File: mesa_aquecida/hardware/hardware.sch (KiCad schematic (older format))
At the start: 29 parts, among them J1 Conn_01x03_Male, J2 Conn_01x04_Male, J3 Conn_01x04_Male, J4 Conn_01x02_Female, J5 Conn_01x02_Male, J6 Conn_01x02_Male, J7 Conn_01x02_Male, J8 Conn_01x02_Male, J9 Conn_01x02_Female, Q1 2N7002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

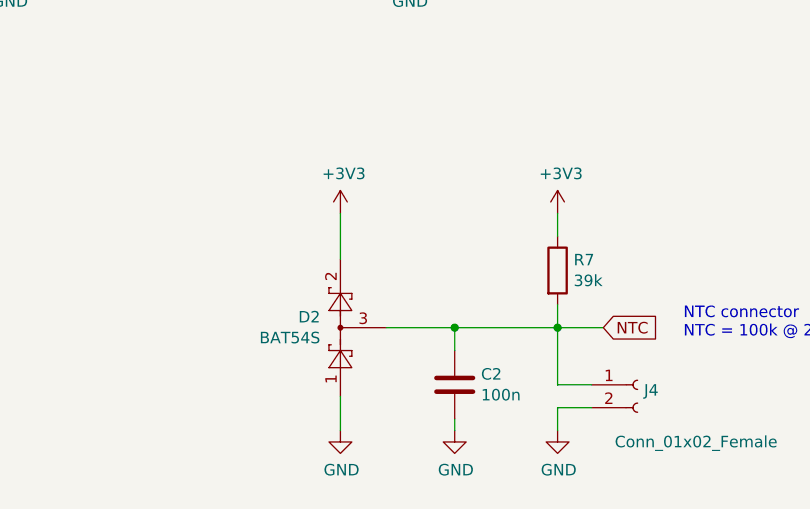
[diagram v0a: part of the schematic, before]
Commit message: updated schematic, removed diodes
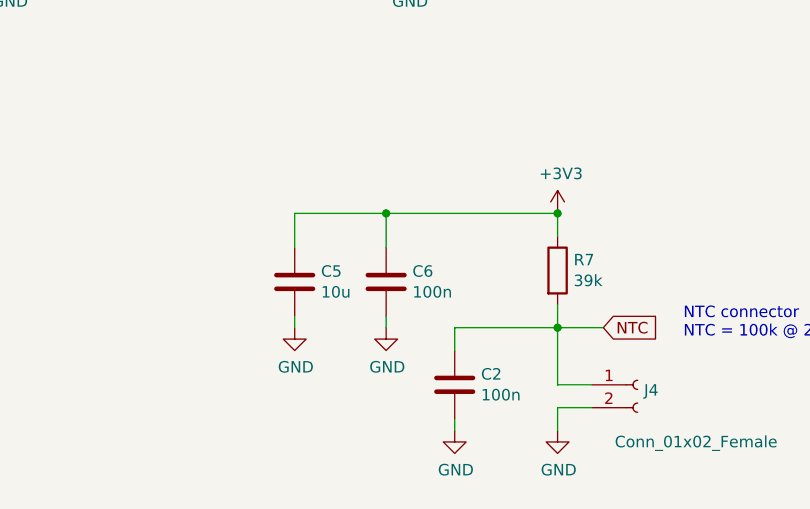
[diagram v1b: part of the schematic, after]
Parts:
- removed D2: BAT54S, Package_TO_SOT_SMD:SOT-23, symbol Diode:BAT54S
- added C5: 10u, symbol Device:C
- added C6: 100n, symbol Device:C
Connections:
- net +3V3: now also C5.1, C6.1
- net GND: now also C5.2, C6.2
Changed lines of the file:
@@
 	1300 5400 1300 5850
-$Comp
-L Diode:BAT54S D2
-U 1 1 6119E775
-P 4100 5950
-F 0 "D2" V 4146 6038 50  0000 L CNN
-F 1 "BAT54S" V 4055 6038 50  0000 L CNN
-F 2 "Package_TO_SOT_SMD:SOT-23" H 4175 6075 50  0001 L CNN
-F 3 "https://www.diodes.com/assets/Datasheets/ds11005.pdf" H 3980 5950 50  0001 C CNN
-	1    4100 5950
-	0    -1   -1   0
-$EndComp
-$Comp
-L power:+3V3 #PWR012
-U 1 1 611A238D
-P 4100 5450
-F 0 "#PWR012" H 4100 5300 50  0001 C CNN
-F 1 "+3V3" H 4115 5623 50  0000 C CNN
-F 2 "" H 4100 5450 50  0001 C CNN
-F 3 "" H 4100 5450 50  0001 C CNN
-	1    4100 5450
-	1    0    0    -1
-$EndComp
-$Comp
-L power:GND #PWR013
-U 1 1 611A28CE
-P 4100 6400
-F 0 "#PWR013" H 4100 6150 50  0001 C CNN
-F 1 "GND" H 4105 6227 50  0000 C CNN
-F 2 "" H 4100 6400 50  0001 C CNN
-F 3 "" H 4100 6400 50  0001 C CNN
-	1    4100 6400
-	1    0    0    -1
-$EndComp
-Wire Wire Line
-	4100 6250 4100 6400
 $Comp
 L Transistor_FET:IRF540N Q2
@@
 	5050 5550 5050 5450
 Wire Wire Line
-	4100 5650 4100 5450
-Wire Wire Line
 	5050 5850 5050 5950
 Connection ~ 5050 5950
@@
 Wire Wire Line
 	5900 3250 6150 3250
-Wire Wire Line
-	4300 5950 4600 5950
 $Comp
 L Device:C C2
@@
 Wire Wire Line
 	4600 6050 4600 5950
-Connection ~ 4600 5950
 Wire Wire Line
 	4600 5950 5050 5950
@@
 Wire Wire Line
 	2900 3650 2400 3650
+$Comp
+L Device:C C6
+U 1 1 61175D0A
+P 4300 5750
+F 0 "C6" H 4415 5796 50  0000 L CNN
+F 1 "100n" H 4415 5705 50  0000 L CNN
+F 2 "" H 4338 5600 50  0001 C CNN
+F 3 "~" H 4300 5750 50  0001 C CNN
+	1    4300 5750
+	1    0    0    -1
+$EndComp
+$Comp
+L Device:C C5
+U 1 1 61176977
+P 3900 5750
+F 0 "C5" H 4015 5796 50  0000 L CNN
+F 1 "10u" H 4015 5705 50  0000 L CNN
+F 2 "" H 3938 5600 50  0001 C CNN
+F 3 "~" H 3900 5750 50  0001 C CNN
+	1    3900 5750
+	1    0    0    -1
+$EndComp
+$Comp
+L power:GND #PWR013
+U 1 1 61176CDE
+P 4300 5950
+F 0 "#PWR013" H 4300 5700 50  0001 C CNN
+F 1 "GND" H 4305 5777 50  0000 C CNN
+F 2 "" H 4300 5950 50  0001 C CNN
+F 3 "" H 4300 5950 50  0001 C CNN
+	1    4300 5950
+	1    0    0    -1
+$EndComp
+$Comp
+L power:GND #PWR012
+U 1 1 61176FB0
+P 3900 5950
+F 0 "#PWR012" H 3900 5700 50  0001 C CNN
+F 1 "GND" H 3905 5777 50  0000 C CNN
+F 2 "" H 3900 5950 50  0001 C CNN
+F 3 "" H 3900 5950 50  0001 C CNN
+	1    3900 5950
+	1    0    0    -1
+$EndComp
+Wire Wire Line
+	4300 5600 4300 5450
+Wire Wire Line
+	4300 5450 5050 5450
+Connection ~ 5050 5450
+Wire Wire Line
+	4300 5450 3900 5450
+Wire Wire Line
+	3900 5450 3900 5600
+Connection ~ 4300 5450
+Wire Wire Line
+	3900 5900 3900 5950
+Wire Wire Line
+	4300 5900 4300 5950
 $EndSCHEMATC

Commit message: Updated PCB
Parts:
- removed J1: Conn_01x03_Male, symbol Connector:Conn_01x03_Male
- removed J9: Conn_01x02_Female, symbol Connector:Conn_01x02_Female
- added HS1: Heatsink, Heatsink:Heatsink_Fischer_SK104-STCB_35x13mm__2xDrill3.5mm_ScrewM3, symbol Mechanical:Heatsink
- added J1, J10: Conn_01x04_Male, Connector_PinHeader_2.54mm:PinHeader_1x04_P2.54mm_Vertical, symbol Connector:Conn_01x04_Male
- added J9: Screw_Terminal_01x03, TerminalBlock:TerminalBlock_bornier-3_P5.08mm, symbol Connector:Screw_Terminal_01x03
- added SW1, SW2, SW3: SW_MEC_5E, Button_Switch_THT:SW_PUSH_6mm, symbol Switch:SW_Push
- C1, C2, C3, C4, C5, C6: footprint (none) -> Capacitor_SMD:C_0805_2012Metric_Pad1.18x1.45mm_HandSolder
- D1, D3: footprint (none) -> Diode_SMD:D_SMB
- J2, J3: footprint (none) -> Connector_PinHeader_2.54mm:PinHeader_1x04_P2.54mm_Vertical
- J4, J5, J6, J7, J8: footprint (none) -> Connector_PinHeader_2.54mm:PinHeader_1x02_P2.54mm_Vertical
- R1, R2, R3, R4, R5, R6, R9: footprint (none) -> Resistor_SMD:R_0805_2012Metric_Pad1.20x1.40mm_HandSolder
- R7: value 39k -> 62k; footprint (none) -> Resistor_SMD:R_0805_2012Metric_Pad1.20x1.40mm_HandSolder
- R8: value 10k -> 500R; footprint (none) -> Resistor_SMD:R_0805_2012Metric_Pad1.20x1.40mm_HandSolder
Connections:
- net +12V: now also J9.1 (Pin_1)
- net GND: now also J1.4 (Pin_4), J9.3 (Pin_3)
- net NTC: now also U1.5 (ADC10CLK/VREF-/VeREF-/CAOUT/CA3/A3/P1.3); no longer U1.4 (TA0.1/CA2/A2/P1.2)
- net at R6.2, U1.10 (P2.2): now also J1.3 (Pin_3)
- net at R2.2, U1.8 (P2.0): now also J1.1 (Pin_1)
- net at R4.2, U1.9 (P2.1): now also J1.2 (Pin_2)
- net at D3.1 (K), Q2.2 (D): now also J9.2 (Pin_2)
- new net: J10.1 (Pin_1), SW1.1
- new net: J10.2 (Pin_2), SW2.1
- new net: J10.3 (Pin_3), SW3.1
- new net GND1: J10.4 (Pin_4), SW1.2, SW2.2, SW3.2
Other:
- note added: "Buttons Board"
- note added: "NTC connector\nNTC = 152k @ 15°"
- note removed: "NTC connector\nNTC = 100k @ 20°"
- moved on the sheet: C2, C5, C6, D3, J2, J4, Q1, Q2, R3, R5, R7, R8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

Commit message: Created pcb
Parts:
- removed J2: Conn_01x04_Male, Connector_PinHeader_2.54mm:PinHeader_1x04_P2.54mm_Vertical, symbol Connector:Conn_01x04_Male
- added H1, H2, H3, H4: MountingHole, MountingHole:MountingHole_4.3mm_M4, symbol Mechanical:MountingHole
- added J11: Screw_Terminal_01x02, TerminalBlock:TerminalBlock_bornier-2_P5.08mm, symbol Connector:Screw_Terminal_01x02
- added J12, J2: Conn_01x02_Female, Connector_PinHeader_2.54mm:PinHeader_1x02_P2.54mm_Vertical, symbol Connector:Conn_01x02_Female
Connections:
- net +12V: now also J11.2 (Pin_2)
- net +5V: now also J2.2 (Pin_2)
- net GND: now also J2.1 (Pin_1)
- net NTC: now also U1.2 (TA0CLK/ACLK/CA0/A0/P1.0); no longer U1.5 (ADC10CLK/VREF-/VeREF-/CAOUT/CA3/A3/P1.3)
- net POWER: now also U1.5 (ADC10CLK/VREF-/VeREF-/CAOUT/CA3/A3/P1.3); no longer U1.13 (P2.5)
- net SCL: now also R3.2, J12.2 (Pin_2); no longer R5.2
- net SDA: now also R5.2, J12.1 (Pin_1); no longer R3.2
- net at D3.1 (K), Q2.2 (D): now also J11.1 (Pin_1); no longer J9.2 (Pin_2)
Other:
- moved on the sheet: J5, J6, J7, J8, J9

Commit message: Added ntc table
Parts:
- C1: value 100n -> 1n
- R7: value 62k -> 82k
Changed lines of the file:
@@
 P 2650 4100
 F 0 "C1" H 2765 4146 50  0000 L CNN
-F 1 "100n" H 2765 4055 50  0000 L CNN
+F 1 "1n" H 2765 4055 50  0000 L CNN
 F 2 "Capacitor_SMD:C_0805_2012Metric_Pad1.18x1.45mm_HandSolder" H 2688 3950 50  0001 C CNN
 F 3 "~" H 2650 4100 50  0001 C CNN
@@
 P 6400 5000
 F 0 "R7" H 6470 5046 50  0000 L CNN
-F 1 "62k" H 6470 4955 50  0000 L CNN
+F 1 "82k" H 6470 4955 50  0000 L CNN
 F 2 "Resistor_SMD:R_0805_2012Metric_Pad1.20x1.40mm_HandSolder" V 6330 5000 50  0001 C CNN
 F 3 "~" H 6400 5000 50  0001 C CNN

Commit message: Updated software
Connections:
- net +3V3: now also R8.2
- net GND: no longer R8.2
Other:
- moved on the sheet: R8
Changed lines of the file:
@@
 	9100 4800 9100 5050
 Connection ~ 9100 4800
-Wire Wire Line
-	8800 5250 8450 5250
 $Comp
 L Device:R R8
 U 1 1 611F5185
-P 8450 5450
-F 0 "R8" H 8520 5496 50  0000 L CNN
-F 1 "500R" H 8520 5405 50  0000 L CNN
-F 2 "Resistor_SMD:R_0805_2012Metric_Pad1.20x1.40mm_HandSolder" V 8380 5450 50  0001 C CNN
-F 3 "~" H 8450 5450 50  0001 C CNN
-	1    8450 5450
-	1    0    0    -1
+P 8450 4900
+F 0 "R8" H 8520 4946 50  0000 L CNN
+F 1 "500R" H 8520 4855 50  0000 L CNN
+F 2 "Resistor_SMD:R_0805_2012Metric_Pad1.20x1.40mm_HandSolder" V 8380 4900 50  0001 C CNN
+F 3 "~" H 8450 4900 50  0001 C CNN
+	1    8450 4900
+	-1   0    0    1
 $EndComp
 $Comp
@@
 	1    0    0    -1
 $EndComp
-$Comp
-L power:GND #PWR025
-U 1 1 611FA791
-P 8450 5650
-F 0 "#PWR025" H 8450 5400 50  0001 C CNN
-F 1 "GND" H 8455 5477 50  0000 C CNN
-F 2 "" H 8450 5650 50  0001 C CNN
-F 3 "" H 8450 5650 50  0001 C CNN
-	1    8450 5650
-	1    0    0    -1
-$EndComp
-Wire Wire Line
-	8450 5250 8450 5300
-Wire Wire Line
-	8450 5600 8450 5650
 Wire Wire Line
 	9100 5450 9100 5650
@@
 Text GLabel 8200 5250 0    50   Input ~ 0
 POWER
-Wire Wire Line
-	8200 5250 8450 5250
-Connection ~ 8450 5250
 $Comp
 L pspice:DIODE D3
@@
 Wire Wire Line
 	9700 3950 9700 4300
+$Comp
+L power:+3V3 #PWR0104
+U 1 1 6127A009
+P 8450 4600
+F 0 "#PWR0104" H 8450 4450 50  0001 C CNN
+F 1 "+3V3" H 8465 4773 50  0000 C CNN
+F 2 "" H 8450 4600 50  0001 C CNN
+F 3 "" H 8450 4600 50  0001 C CNN
+	1    8450 4600
+	1    0    0    -1
+$EndComp
+Wire Wire Line
+	8200 5250 8450 5250
+Wire Wire Line
+	8450 4600 8450 4750
+Wire Wire Line
+	8450 5050 8450 5250
+Connection ~ 8450 5250
+Wire Wire Line
+	8450 5250 8800 5250
 $EndSCHEMATC
